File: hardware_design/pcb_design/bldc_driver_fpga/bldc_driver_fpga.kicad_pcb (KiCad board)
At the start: 2 copper layers, 68.6 x 53.3 mm, 71 parts, among them IC1 DRV8300NRGE, IC2 INA180A2, IC3 INA180A2, J1 Voltage Bus In, J2 Power, J3 Digital 1, J4 Digital 2, J5 Analog, J6 Motor Out, J7 Hall/Encoder, Q1 CSD17578Q5A, Q2 CSD17578Q5A, Q3 CSD17578Q5A, Q4 CSD17578Q5A, Q5 CSD17578Q5A, Q6 CSD17578Q5A, U1 LM339

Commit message: Tested inverter, works. Tested ADC triggering, mostly works except not sure if current is correct. Found issue with back EMF causing FPGA to crash.
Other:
- net class Default removed

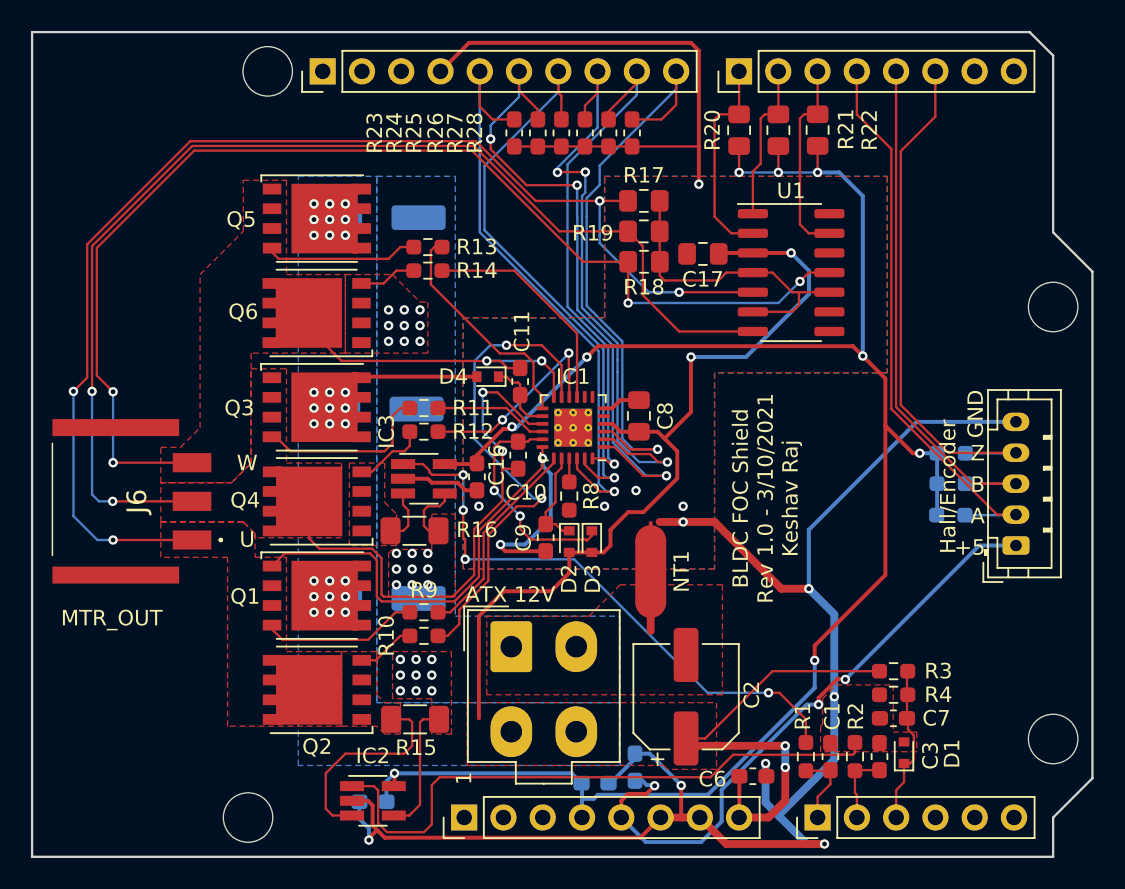
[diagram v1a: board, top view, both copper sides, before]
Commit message: Implemented pure sinewave drive from programmable logic. Set up time base generator for ADC.
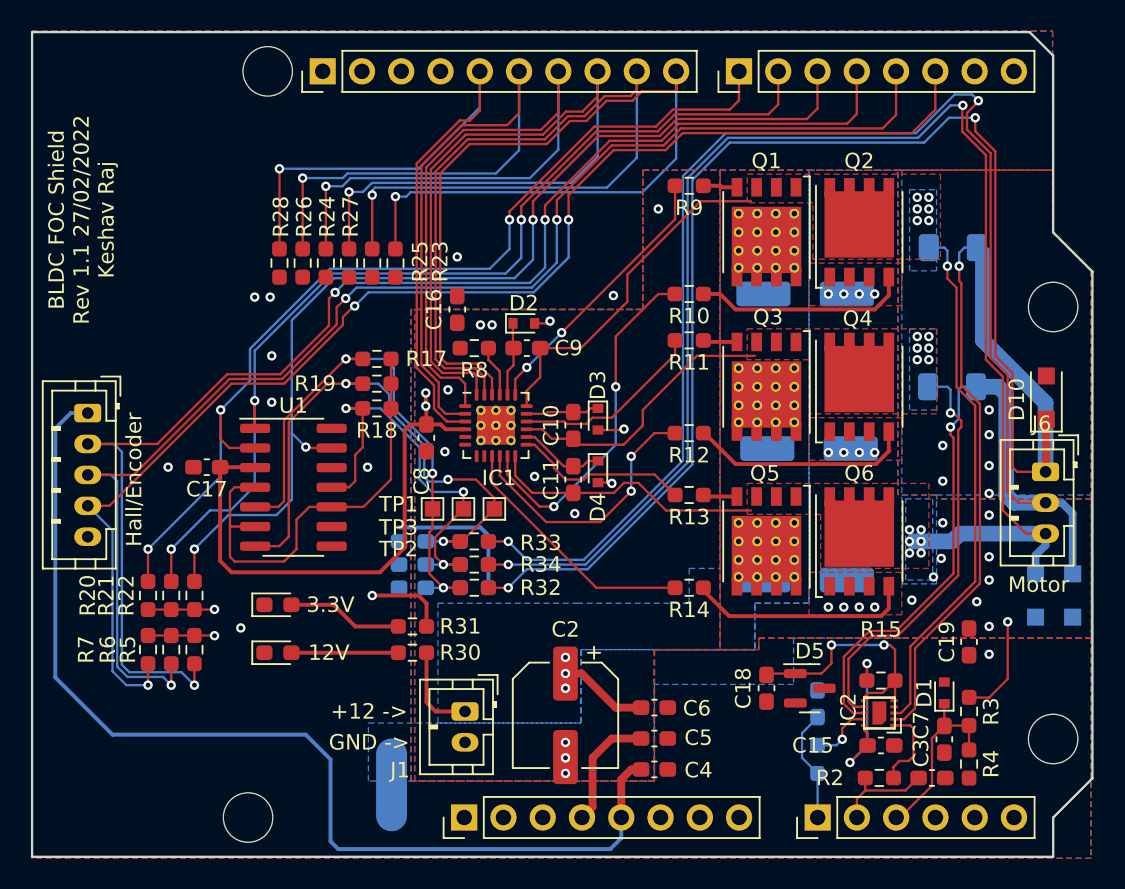
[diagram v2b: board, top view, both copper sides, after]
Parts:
- removed IC3: INA180A2, Package_TO_SOT_SMD:SOT-23-5_HandSoldering
- added C18: 0.1uF 16V, Capacitor_SMD:C_0603_1608Metric_Pad1.08x0.95mm_HandSolder, F.Cu at (107.5, 58.0)
- added C19: 470pF 16V, Capacitor_SMD:C_0603_1608Metric_Pad1.08x0.95mm_HandSolder, F.Cu at (120.6, 55.0)
- added C20: 0.47uF 16V, Capacitor_SMD:C_0603_1608Metric_Pad1.08x0.95mm_HandSolder, B.Cu at (84.6, 51.5)
- added C21: 0.47uF 16V, Capacitor_SMD:C_0603_1608Metric_Pad1.08x0.95mm_HandSolder, B.Cu at (84.6, 48.5)
- added C22: 0.47uF 16V, Capacitor_SMD:C_0603_1608Metric_Pad1.08x0.95mm_HandSolder, B.Cu at (84.6, 50.0)
- added D10: MBR0580, Diode_SMD:D_SOD-123F, F.Cu at (125.6, 39.2)
- added D5: 1V, Package_TO_SOT_SMD:SOT-23, F.Cu at (110.3, 58.0)
- added D6: 3V3Ind, LED_SMD:LED_0603_1608Metric_Pad1.05x0.95mm_HandSolder, F.Cu at (75.9, 55.7)
- added D7: 5VInd, LED_SMD:LED_0603_1608Metric_Pad1.05x0.95mm_HandSolder, F.Cu at (75.9, 52.6)
- added D8: MBR0580, Diode_SMD:D_SOD-123F, B.Cu at (124.9, 52.0)
- added D9: MBR0580, Diode_SMD:D_SOD-123F, B.Cu at (127.3, 52.0)
- added R29: 0.02R, Resistor_SMD:R_1206_3216Metric_Pad1.30x1.75mm_HandSolder, B.Cu at (119.5, 38.5)
- added R30: 5.1k, Resistor_SMD:R_0603_1608Metric_Pad0.98x0.95mm_HandSolder, F.Cu at (84.6, 55.7)
- added R31: 680R, Resistor_SMD:R_0603_1608Metric_Pad0.98x0.95mm_HandSolder, F.Cu at (84.6, 54.0)
- added R32: 1.2k, Resistor_SMD:R_0603_1608Metric_Pad0.98x0.95mm_HandSolder, F.Cu at (88.6, 51.5)
- added R33: 1.2k, Resistor_SMD:R_0603_1608Metric_Pad0.98x0.95mm_HandSolder, F.Cu at (88.6, 48.5)
- added R34: 1.2k, Resistor_SMD:R_0603_1608Metric_Pad0.98x0.95mm_HandSolder, F.Cu at (88.6, 50.0)
- added R35: 1.2k, Resistor_SMD:R_0603_1608Metric_Pad0.98x0.95mm_HandSolder, B.Cu at (88.6, 51.5)
- added R36: 1.2k, Resistor_SMD:R_0603_1608Metric_Pad0.98x0.95mm_HandSolder, B.Cu at (88.6, 48.5)
- added R37: 1.2k, Resistor_SMD:R_0603_1608Metric_Pad0.98x0.95mm_HandSolder, B.Cu at (88.6, 50.0)
- added TP1: TestPoint, TestPoint:TestPoint_Pad_1.0x1.0mm, F.Cu at (85.9, 46.4)
- added TP2: TestPoint, TestPoint:TestPoint_Pad_1.0x1.0mm, F.Cu at (89.9, 46.4)
- added TP3: TestPoint, TestPoint:TestPoint_Pad_1.0x1.0mm, F.Cu at (87.9, 46.4)
- C1: footprint Capacitor_SMD:C_0603_1608Metric_Pad1.05x0.95mm_HandSolder -> Capacitor_SMD:C_0603_1608Metric_Pad1.08x0.95mm_HandSolder; moved to B.Cu
- C10, C11, C3, C6, C7, C9: footprint Capacitor_SMD:C_0603_1608Metric_Pad1.05x0.95mm_HandSolder -> Capacitor_SMD:C_0603_1608Metric_Pad1.08x0.95mm_HandSolder
- C15, C4, C5: footprint Capacitor_SMD:C_0603_1608Metric_Pad1.05x0.95mm_HandSolder -> Capacitor_SMD:C_0603_1608Metric_Pad1.08x0.95mm_HandSolder; moved to F.Cu
- C16: value 0.1uF 16V -> 470pF 16V; footprint Capacitor_SMD:C_0603_1608Metric_Pad1.05x0.95mm_HandSolder -> Capacitor_SMD:C_0603_1608Metric_Pad1.08x0.95mm_HandSolder
- C17, C8: footprint Capacitor_SMD:C_0805_2012Metric_Pad1.15x1.40mm_HandSolder -> Capacitor_SMD:C_0603_1608Metric_Pad1.08x0.95mm_HandSolder
- IC1: footprint Package_DFN_QFN:VQFN-24-1EP_4x4mm_P0.5mm_EP2.45x2.45mm_ThermalVias -> bldc_driver_fpga:VQFN-24-1EP_4x4mm_P0.5mm_EP2.45x2.45mm_ThermalViasBig
- IC2: value INA180A2 -> INA2181A2IDSQR; footprint Package_TO_SOT_SMD:SOT-23-5_HandSoldering -> bldc_driver_fpga:WSON-10-1EP_2.0x2.0mm_P0.4mm_EP0.9x1.5mm
- J1: value Voltage Bus In -> Power In; footprint Connector_Molex:Molex_Mini-Fit_Jr_5566-04A_2x02_P4.20mm_Vertical -> Connector_JST:JST_PH_B2B-PH-K_1x02_P2.00mm_Vertical
- J6: footprint SamacSys_Parts:1054301103 -> Connector_JST:JST_PH_B3B-PH-K_1x03_P2.00mm_Vertical
- NT1: moved to B.Cu
- Q1, Q3, Q5: footprint bldc_driver_fpga:TDSON-8-1_HandSoldering_SGD -> bldc_driver_fpga:TDSON-8-1_HandSolderingVias_SGD
- R1: value 1.6k -> 2.2k; moved to B.Cu
- R15: value 20m -> 2.2k; footprint Resistor_SMD:R_1206_3216Metric_Pad1.30x1.75mm_HandSolder -> Resistor_SMD:R_0603_1608Metric_Pad0.98x0.95mm_HandSolder
- R16: value 20m -> 0.02R; moved to B.Cu
- R17, R18, R19: value 4k7 -> 100k; footprint Resistor_SMD:R_0805_2012Metric_Pad1.15x1.40mm_HandSolder -> Resistor_SMD:R_0603_1608Metric_Pad0.98x0.95mm_HandSolder
- R2: value 1.6k -> 2.2k
- R20, R21, R22: footprint Resistor_SMD:R_0805_2012Metric_Pad1.15x1.40mm_HandSolder -> Resistor_SMD:R_0603_1608Metric_Pad0.98x0.95mm_HandSolder
- R23, R24, R25, R26, R27, R28: footprint Resistor_SMD:R_0603_1608Metric_Pad1.05x0.95mm_HandSolder -> Resistor_SMD:R_0603_1608Metric_Pad0.98x0.95mm_HandSolder
- R5, R6, R7: moved to F.Cu
- moved J7 60.6 mm to (63.6, 40.2), turned to -90 degrees
- moved J6 59.9 mm to (125.5, 44.0)
- moved R7 53.5 mm to (67.5, 55.5), turned to -90 degrees
- moved R6 51.6 mm to (69.0, 55.5), turned to -90 degrees
- moved R22 50.3 mm to (70.5, 52.0)
- moved R5 49.7 mm to (70.5, 55.5), turned to -90 degrees
- moved R21 49.5 mm to (69.0, 52.0)
- moved R20 48.7 mm to (67.5, 52.0)
- moved Q2 45.9 mm to (113.5, 28.5), turned to 90 degrees
- moved R16 39.3 mm to (119.5, 29.5)
- moved Q6 38.1 mm to (113.5, 48.5), turned to 90 degrees
- moved Q1 37.4 mm to (107.5, 28.5), turned to -90 degrees
- moved C14 36.3 mm to (110.0, 51.0)
- moved Q4 35.9 mm to (113.5, 38.5), turned to 90 degrees
- moved Q5 35.8 mm to (107.5, 48.5), turned to -90 degrees
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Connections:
- net Net-(J4-Pad4) renamed /HALL_A
- net Net-(J4-Pad5) renamed /HALL_B
- net Net-(J4-Pad6) renamed /HALL_C
- C10 pad 1: /Zerocrossing Detect/V -> /Inverter/V_SW
- C11 pad 1: /Zerocrossing Detect/W -> /Inverter/W_OUT
- C16 pad 1: +3V3 -> GND
- C16 pad 2: GND -> GNDPWR
- C8 pad 2: GND -> GNDPWR
- C9 pad 1: /Zerocrossing Detect/U -> /Inverter/U_SW
- IC1 pad 12: /Zerocrossing Detect/W -> /Inverter/W_OUT
- IC1 pad 15: /Zerocrossing Detect/V -> /Inverter/V_SW
- IC1 pad 18: /Zerocrossing Detect/U -> /Inverter/U_SW
- IC1 pad 25: GND -> GNDPWR
- IC1 pad 5: Net-(IC1-Pad5) -> unconnected-(IC1-Pad5)
- IC1 pad 6: GND -> GNDPWR
- IC1 pad 7: Net-(IC1-Pad7) -> unconnected-(IC1-Pad7)
- IC1 pad 8: Net-(IC1-Pad8) -> unconnected-(IC1-Pad8)
- IC2 pad 2: GND -> /Inverter/U_OUT
- IC2 pad 3: /Inverter/Phase A Current Sense/LS_SOURCE -> /Inverter/U_SW
- IC2 pad 4: GNDPWR -> GND
- IC2 pad 5: +3V3 -> Net-(C18-Pad1)
- J1 pad 1: GNDPWR -> +12V
- J2 pad 1: Net-(J2-Pad1) -> unconnected-(J2-Pad1)
- J2 pad 2: Net-(J2-Pad2) -> unconnected-(J2-Pad2)
- J2 pad 3: Net-(J2-Pad3) -> unconnected-(J2-Pad3)
- J2 pad 8: +12V -> unconnected-(J2-Pad8)
- J3 pad 1: Net-(J3-Pad1) -> unconnected-(J3-Pad1)
- J3 pad 10: /INLC -> /INHA
- J3 pad 2: Net-(J3-Pad2) -> unconnected-(J3-Pad2)
- J3 pad 3: Net-(J3-Pad3) -> unconnected-(J3-Pad3)
- J3 pad 5: /INHA -> /INLC
- J3 pad 6: /INLA -> /INLB
- J3 pad 7: /INHB -> /INLA
- J3 pad 8: /INLB -> /INHC
- J3 pad 9: /INHC -> /INHB
- J4 pad 7: Net-(J4-Pad7) -> unconnected-(J4-Pad7)
- J4 pad 8: Net-(J4-Pad8) -> unconnected-(J4-Pad8)
- J5 pad 4: Net-(J5-Pad4) -> unconnected-(J5-Pad4)
- J5 pad 5: Net-(J5-Pad5) -> unconnected-(J5-Pad5)
- J5 pad 6: Net-(J5-Pad6) -> unconnected-(J5-Pad6)
- J6 pad 1: /Zerocrossing Detect/U -> /Inverter/U_OUT
- J6 pad 2: /Zerocrossing Detect/V -> /Inverter/V_OUT
- J6 pad 3: /Zerocrossing Detect/W -> /Inverter/W_OUT
- Q1 pad 1: /Zerocrossing Detect/U -> /Inverter/U_SW
- Q2 pad 1: /Inverter/Phase A Current Sense/LS_SOURCE -> GNDPWR
- Q2 pad 3: /Zerocrossing Detect/U -> /Inverter/U_SW
- Q3 pad 1: /Zerocrossing Detect/V -> /Inverter/V_SW
- Q4 pad 1: /Inverter/sheet613E4E23/LS_SOURCE -> GNDPWR
- Q4 pad 3: /Zerocrossing Detect/V -> /Inverter/V_SW
- Q5 pad 1: /Zerocrossing Detect/W -> /Inverter/W_OUT
- Q6 pad 3: /Zerocrossing Detect/W -> /Inverter/W_OUT
- R15 pad 1: /Inverter/Phase A Current Sense/LS_SOURCE -> +3V3
- R15 pad 2: GNDPWR -> Net-(C18-Pad1)
- R16 pad 1: /Inverter/sheet613E4E23/LS_SOURCE -> /Inverter/U_SW
- R16 pad 2: GNDPWR -> /Inverter/U_OUT
- R17 pad 1: /Zerocrossing Detect/U -> Net-(C20-Pad1)
- R18 pad 2: /Zerocrossing Detect/W -> Net-(C22-Pad1)
- R19 pad 1: /Zerocrossing Detect/V -> Net-(C21-Pad1)
- R8 pad 2: GND -> GNDPWR
- U1 pad 11: /Zerocrossing Detect/W -> Net-(C22-Pad1)
- U1 pad 5: /Zerocrossing Detect/U -> Net-(C20-Pad1)
- U1 pad 7: /Zerocrossing Detect/V -> Net-(C21-Pad1)
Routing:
- net GND: track 149.0 -> 9.41 mm, vias 12 -> 10
- net /Inverter/U_OUT: track 0.00 -> 135.2 mm, vias 0 -> 3
- net /Inverter/V_OUT: track 0.00 -> 129.7 mm, vias 0 -> 3
- net /Zerocrossing Detect/U: track 118.3 -> 0.00 mm, vias 6 -> 0
- net /Inverter/W_OUT: track 0.00 -> 114.1 mm, vias 0 -> 8
- net /Zerocrossing Detect/V: track 111.9 -> 0.00 mm, vias 4 -> 0
- net /Zerocrossing Detect/W: track 97.8 -> 0.00 mm, vias 6 -> 0
- net +3V3: track 122.5 -> 32.5 mm, vias 9 -> 5
- net +12V: track 126.6 -> 57.2 mm, vias 31 -> 9
- net /Inverter/U_SW: track 0.00 -> 57.1 mm, vias 0 -> 7
- net /Zerocrossing Detect/C: track 13.0 -> 68.6 mm, vias 0 -> 3
- net /Zerocrossing Detect/B: track 10.4 -> 64.2 mm, vias 0 -> 3
- net /HALL_B: track 34.8 -> 87.0 mm, vias 0 -> 3
- net /HALL_C: track 34.5 -> 85.8 mm, vias 0 -> 3
- net /HALL_A: track 37.0 -> 87.4 mm, vias 0 -> 3
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- added copper zone on In1.Cu, net +12V
- added copper zone on In1.Cu, net +3V3
- added copper zone on B.Cu, net /Inverter/U_SW
- added copper zone on F.Cu, net /Inverter/U_SW
- added copper zone on B.Cu, net /Inverter/V_SW
- added copper zone on F.Cu, net /Inverter/V_SW
- added copper zone on B.Cu, net /Inverter/W_OUT
- added copper zone on F.Cu, net /Inverter/W_OUT
- added copper zone on In2.Cu, net GND
- added copper zone on In2.Cu, net GNDPWR
- removed copper zone on F.Cu, net +12V
- removed copper zone on F.Cu, net /Inverter/Phase A Current Sense/LS_SOURCE
- removed copper zone on F.Cu, net /Inverter/sheet613E4E23/LS_SOURCE
- removed copper zone on F.Cu, net /Zerocrossing Detect/U
- removed copper zone on F.Cu, net /Zerocrossing Detect/V
- removed copper zone on F.Cu, net /Zerocrossing Detect/W
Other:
- copper layers 2 -> 4
- board text added: "+12 ->"
- board text added: "12V"
- board text added: "3.3V"
- board text added: "BLDC FOC Shield Rev 1.1 27/02/2022 Keshav Raj"
- board text added: "GND ->"
- board text added: "Motor"
- board text removed: "+5"
- board text removed: "1"
- board text removed: "A"
- board text removed: "ATX 12V"
- board text removed: "B"
- board text removed: "BLDC FOC Shield Rev 1.0 - 3/10/2021 Keshav Raj"
- board text removed: "GND"
- board text removed: "MTR_OUT"
- board text removed: "U"
- board text removed: "W"
- board text removed: "Z"
